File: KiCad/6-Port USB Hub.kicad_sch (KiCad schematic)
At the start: 0 parts

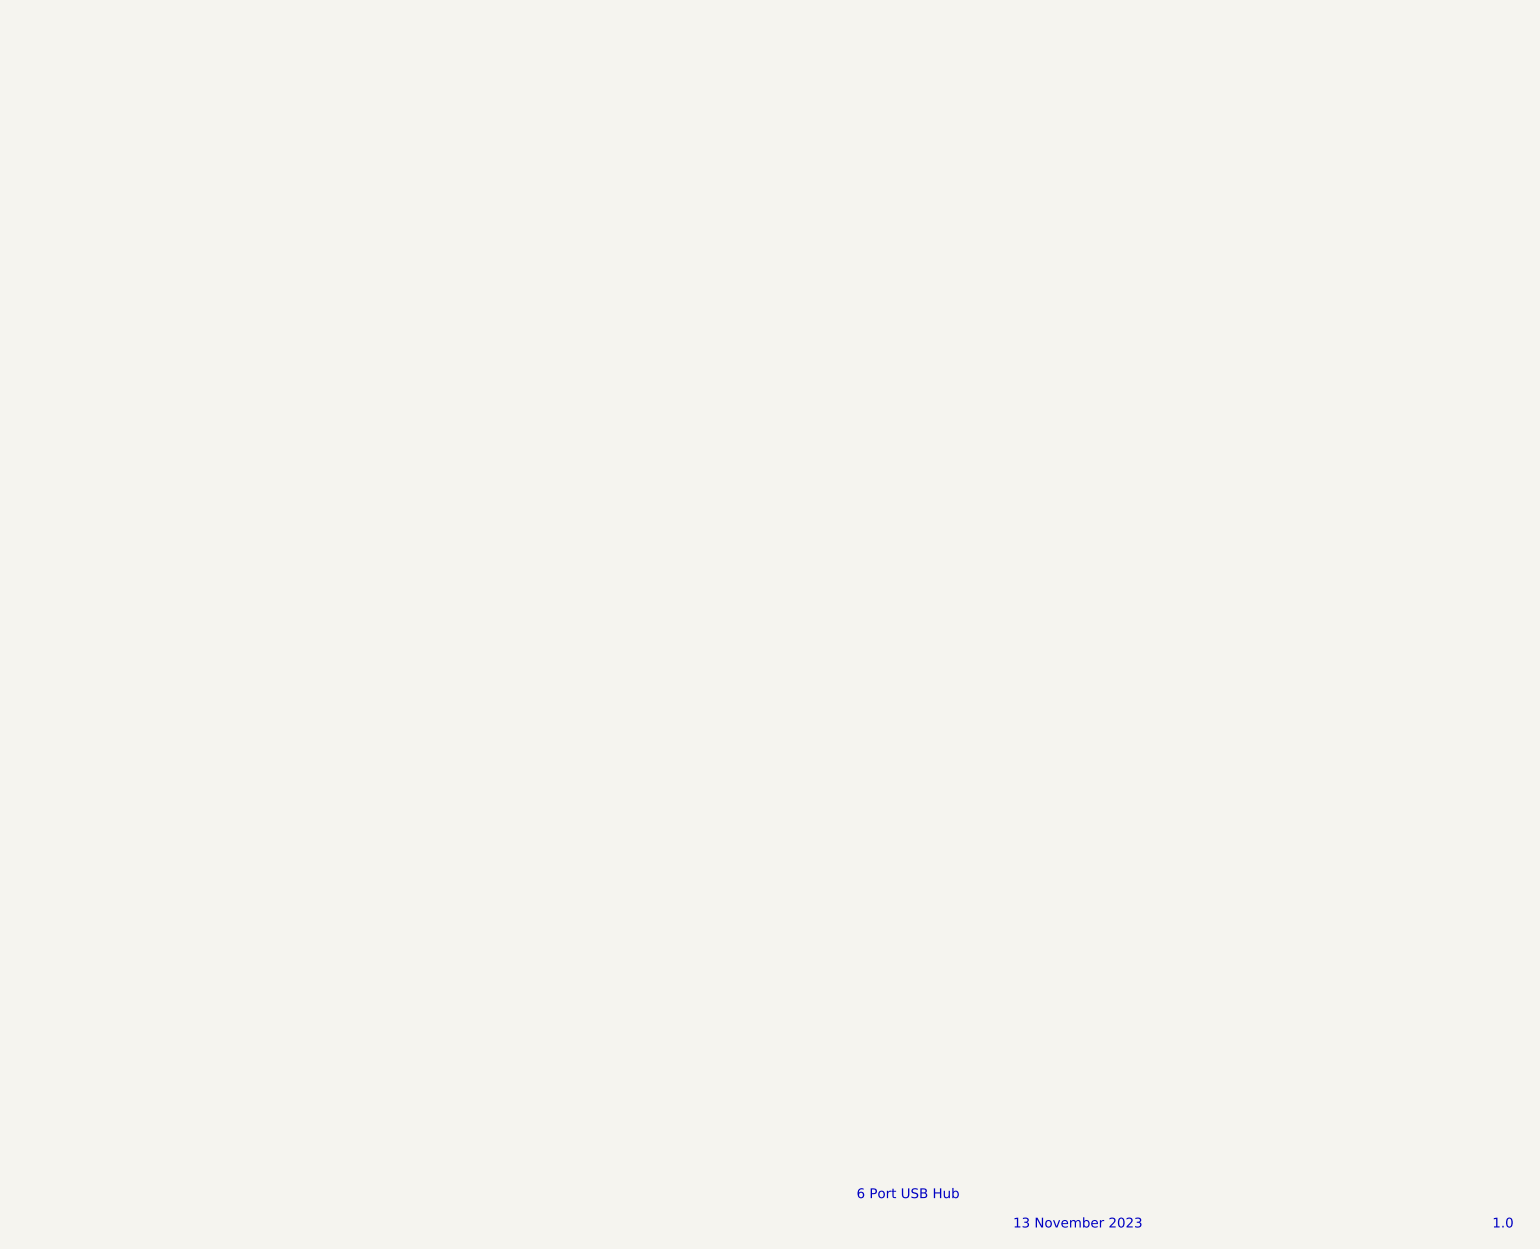
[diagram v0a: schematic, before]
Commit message: added usb controller IC
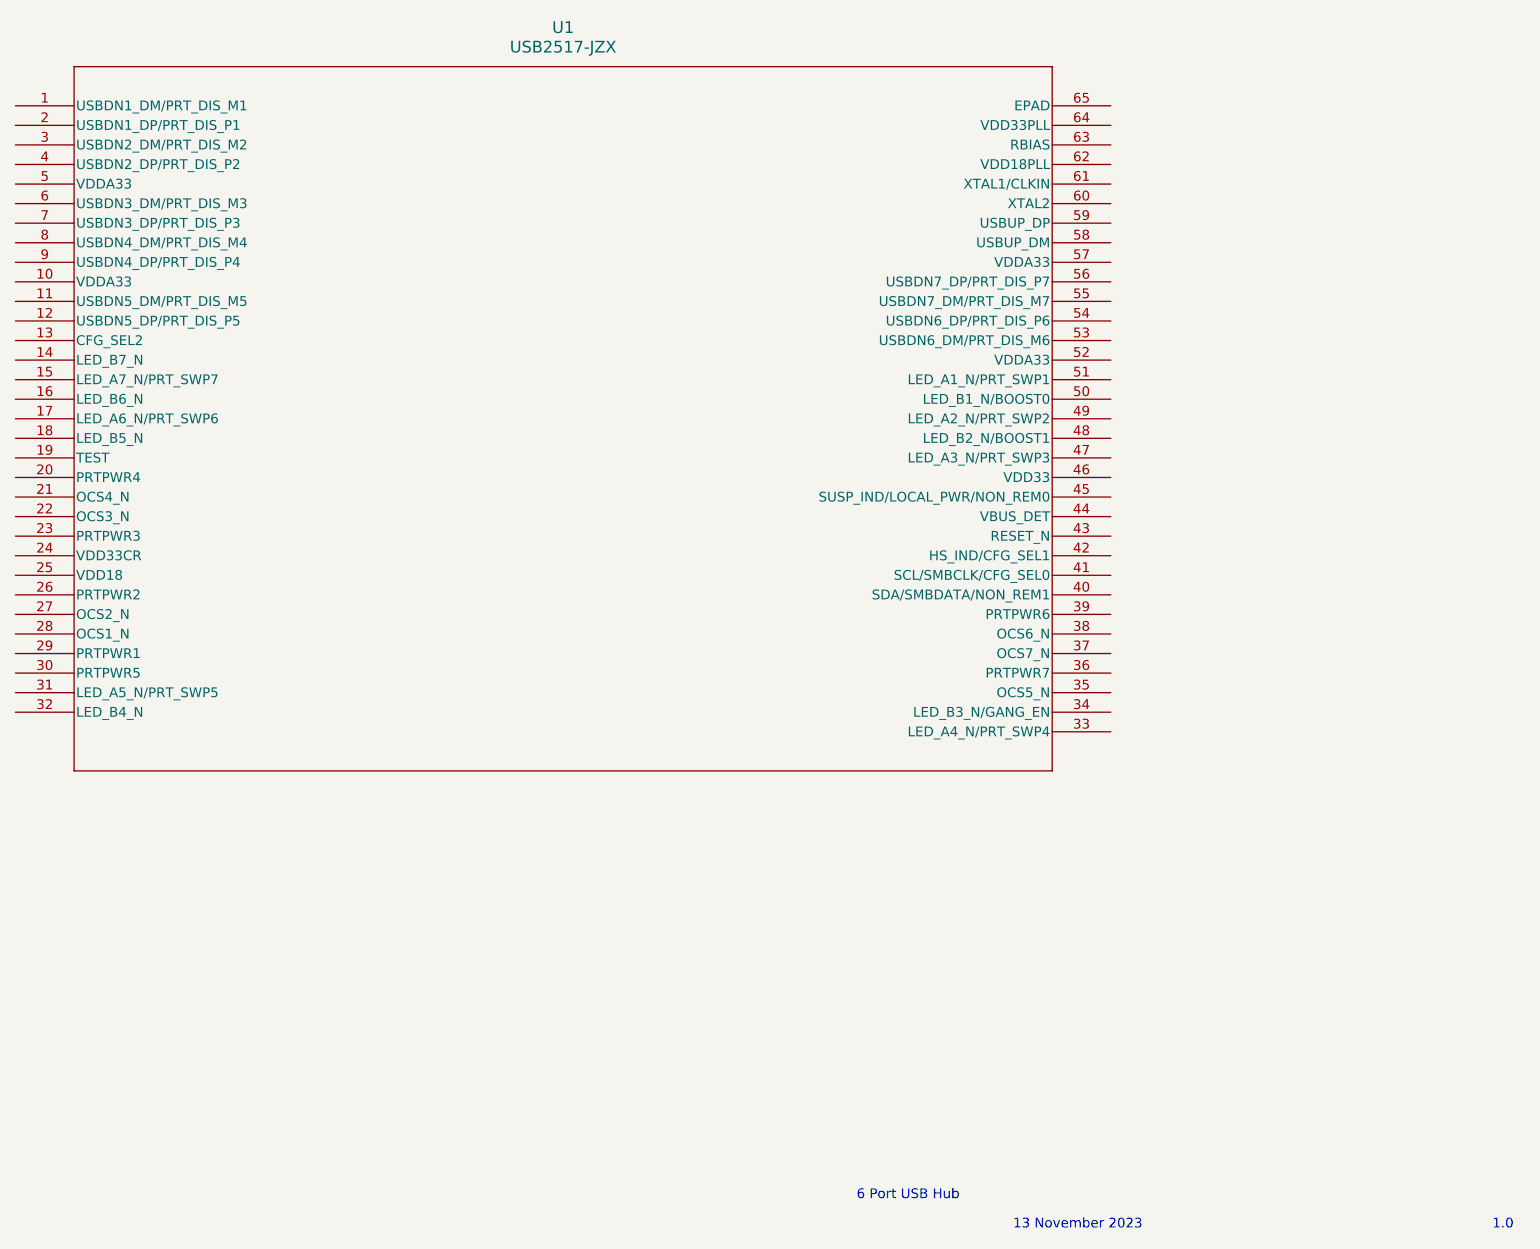
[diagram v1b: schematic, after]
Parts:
- added U1: USB2517-JZX, QFN64_9x9MC_MCH, symbol KiCadLib:USB2517-JZX
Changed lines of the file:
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@@
     (effects (font (size 1.27 1.27)) (justify left bottom))
+  )
+  (symbol (lib_id "KiCadLib:USB2517-JZX") (at 77.47 48.26 0) (unit 1)
+    (in_bom yes) (on_board yes) (dnp no) (fields_autoplaced)
+    (property "Reference" "U1" (at 148.59 38.1 0)
+      (effects (font (size 1.524 1.524)))
+    )
+    (property "Value" "USB2517-JZX" (at 148.59 40.64 0)
+      (effects (font (size 1.524 1.524)))
+    )
+    (property "Footprint" "QFN64_9x9MC_MCH" (at 77.47 48.26 0)
+      (effects (font (size 1.27 1.27) italic) hide)
+    )
+    (property "Datasheet" "USB2517-JZX-TR" (at 77.47 48.26 0)
+      (effects (font (size 1.27 1.27) italic) hide)
+    )
+    (pin "1")
+    (pin "10")
+    (pin "11")
+    (pin "12")
+    (pin "13")
+    (pin "14")
+    (pin "15")
+    (pin "16")
+    (pin "17")
+    (pin "18")
+    (pin "19")
+    (pin "2")
+    (pin "20")
+    (pin "21")
+    (pin "22")
+    (pin "23")
+    (pin "24")
+    (pin "25")
+    (pin "26")
+    (pin "27")
+    (pin "28")
+    (pin "29")
+    (pin "3")
+    (pin "30")
+    (pin "31")
+    (pin "32")
+    (pin "33")
+    (pin "34")
+    (pin "35")
+    (pin "36")
+    (pin "37")
+    (pin "38")
+    (pin "39")
+    (pin "4")
+    (pin "40")
+    (pin "41")
+    (pin "42")
+    (pin "43")
+    (pin "44")
+    (pin "45")
+    (pin "46")
+    (pin "47")
+    (pin "48")
+    (pin "49")
+    (pin "5")
+    (pin "50")
+    (pin "51")
+    (pin "52")
+    (pin "53")
+    (pin "54")
+    (pin "55")
+    (pin "56")
+    (pin "57")
+    (pin "58")
+    (pin "59")
+    (pin "6")
+    (pin "60")
+    (pin "61")
+    (pin "62")
+    (pin "63")
+    (pin "64")
+    (pin "65")
+    (pin "7")
+    (pin "8")
+    (pin "9")
+    (instances
+      (project "6-Port USB Hub"
+        (path "/8fcfbb12-1fd7-4f2b-aff2-d97df2748f4d"
+          (reference "U1") (unit 1)
+        )
+      )
+    )
   )
   (sheet_instances
